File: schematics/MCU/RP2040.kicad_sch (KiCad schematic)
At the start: 37 parts, among them J2 Conn_ARM_SWD_TagConnect_TC203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, Q1 2N7002VC-7, SW1 SWITCH, U3 GD25LQ128DYIGR

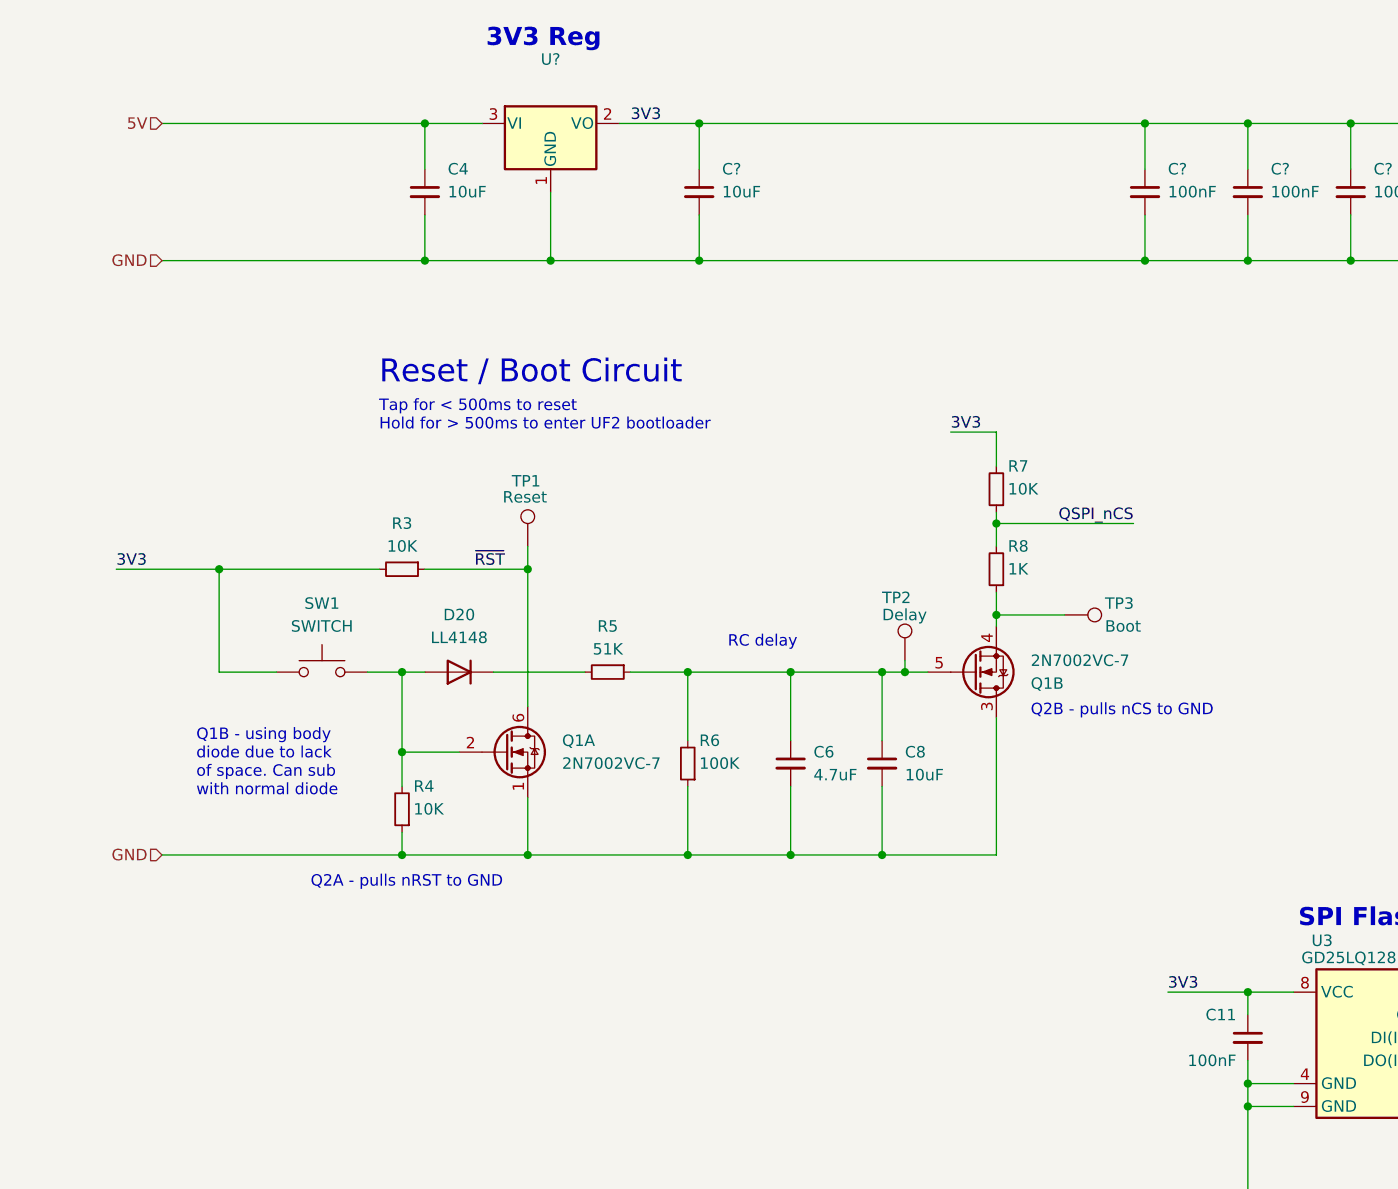
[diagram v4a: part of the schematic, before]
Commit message: copy used footprints into lib, link 3D models
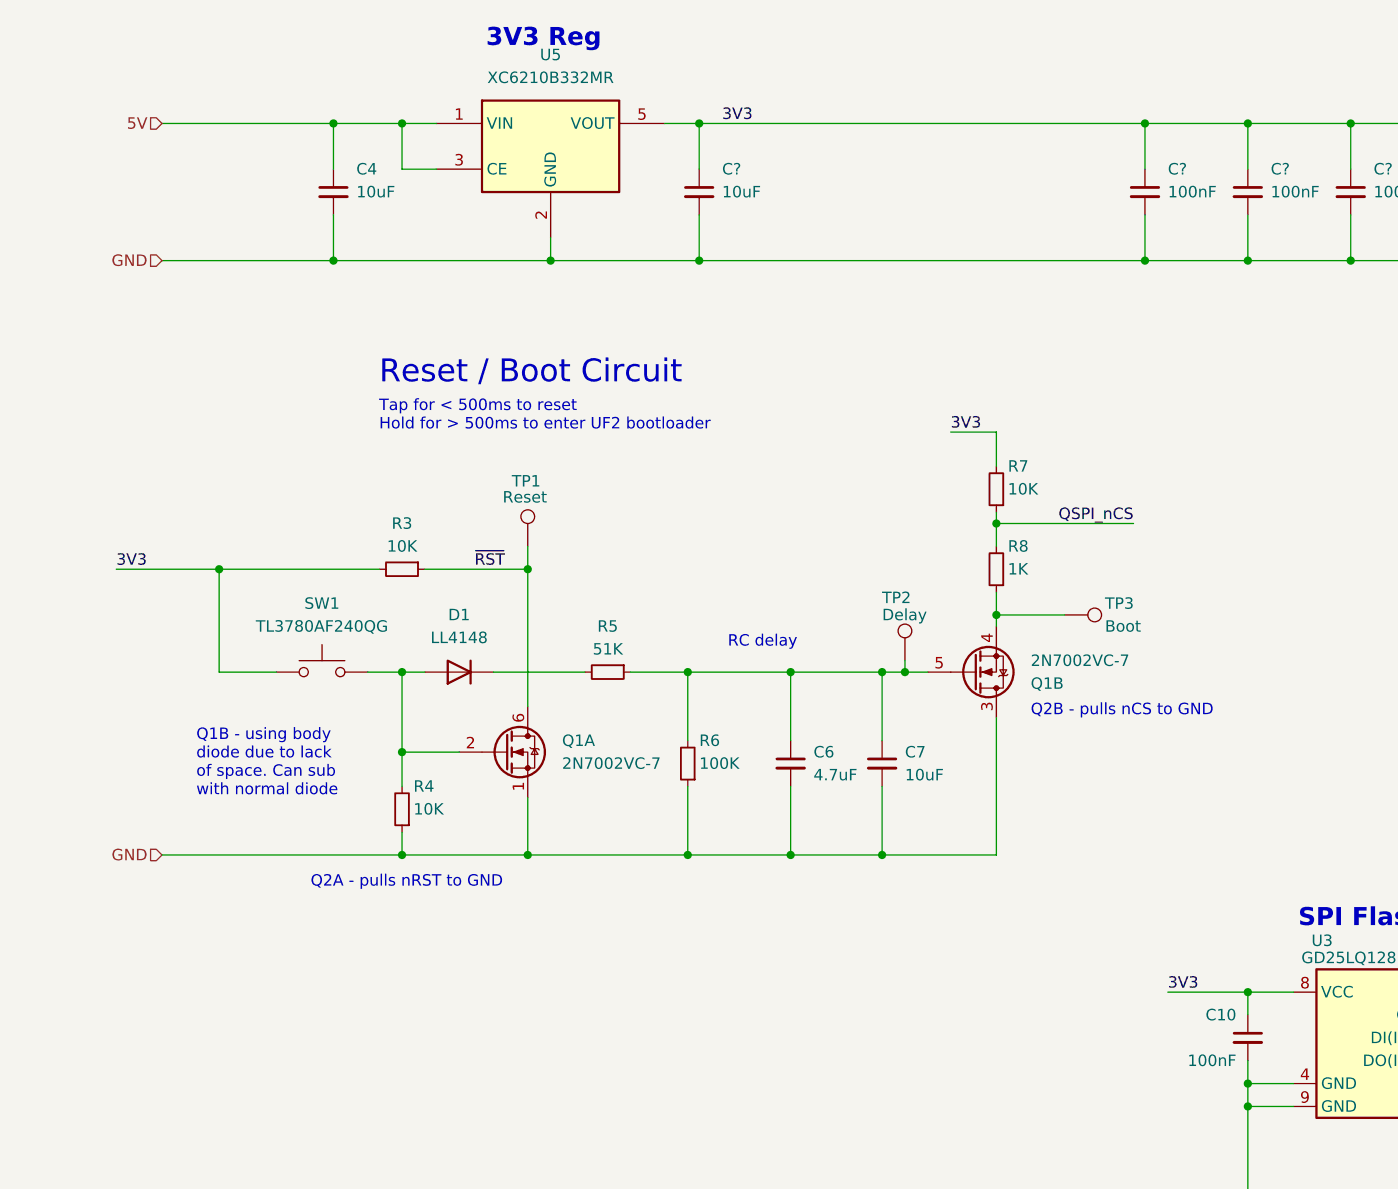
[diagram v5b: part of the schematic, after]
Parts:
- removed U?: XC6206PxxxMR-Regulator_Linear, Package_TO_SOT_SMD:SOT-23, symbol kicad-keyboard-parts:XC6206PxxxMR-Regulator_Linear
- added U5: XC6210B332MR, Package_TO_SOT_SMD:SOT-23-5, symbol Regulator_Linear:XC6210B332MR
- SW1: value SWITCH -> TL3780AF240QG; footprint (none) -> Mad_Footprints:SW_TL3780AF240QG; MPN (none) -> TL3780AF240QG; Manufacturer (none) -> E-Switch; Price (none) -> $0.41; Rating (none) -> SWITCH TACTILE SPST-NO 0.05A 12V; Supplier (none) -> Digikey; Supplier PN (none) -> EG5393CT-ND
- renumbered C11 to C10, C8 to C7, D20 to D1
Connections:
- net 5V: now also U5.1 (VIN), U5.3 (CE)
- net GND: now also U5.2 (GND)
- net IOVDD: now also U5.5 (VOUT)
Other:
- moved on the sheet: C4

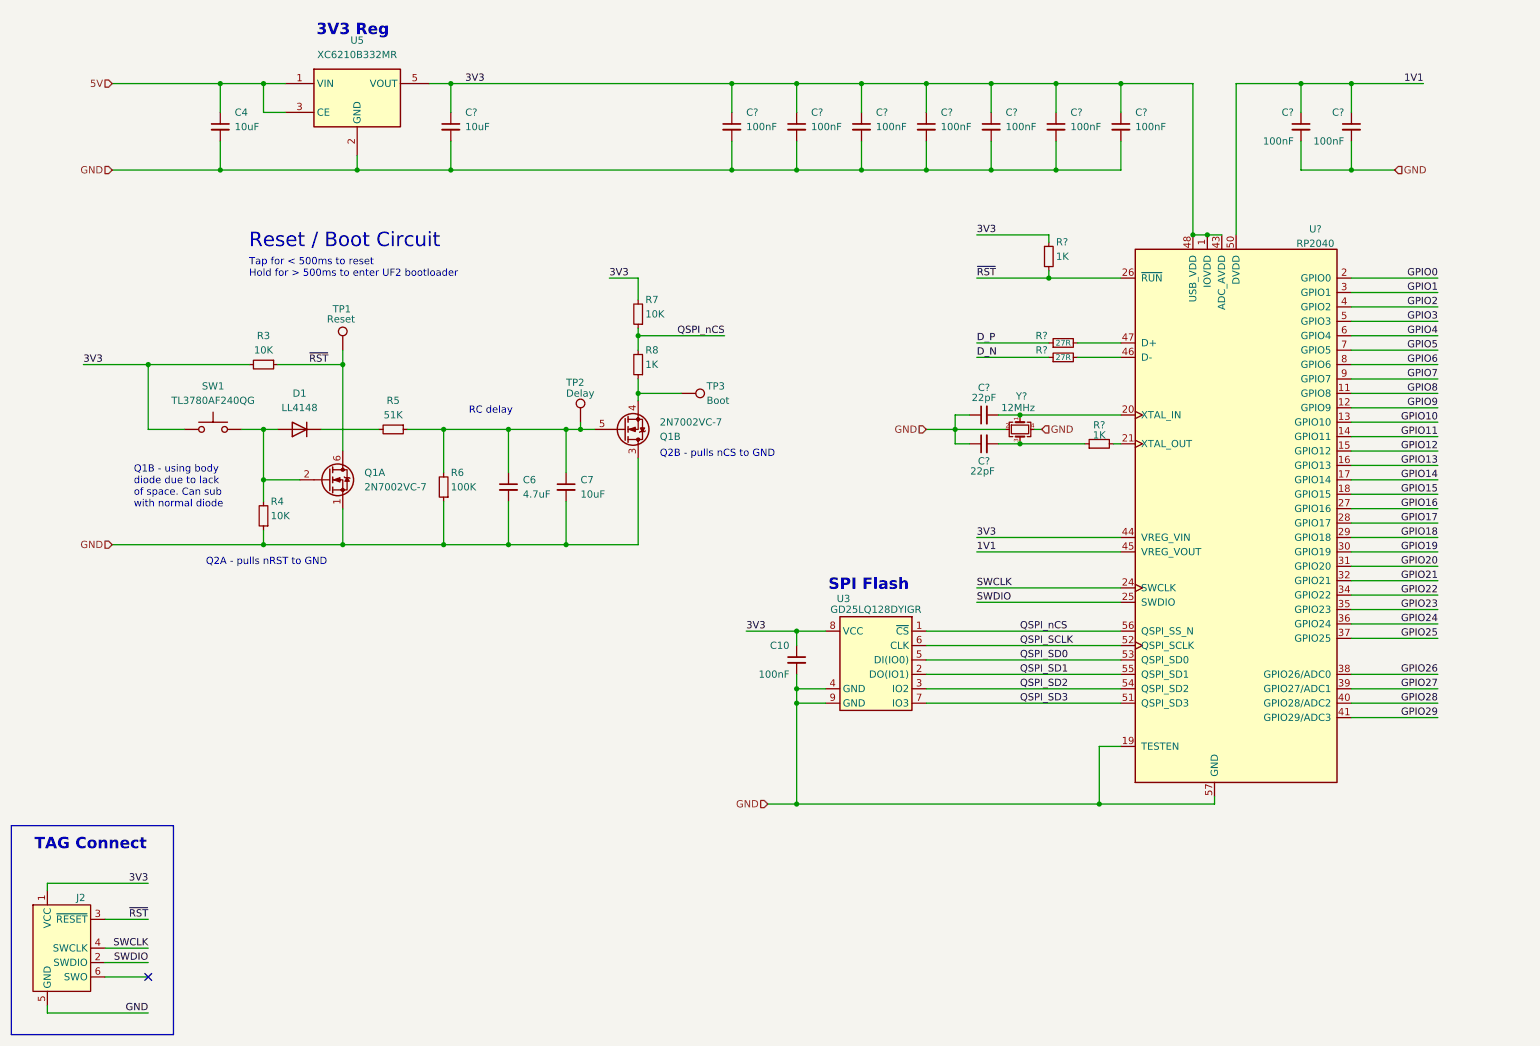
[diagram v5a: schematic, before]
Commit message: Update RP2040, rename bom only footprint, add mechanical footprint
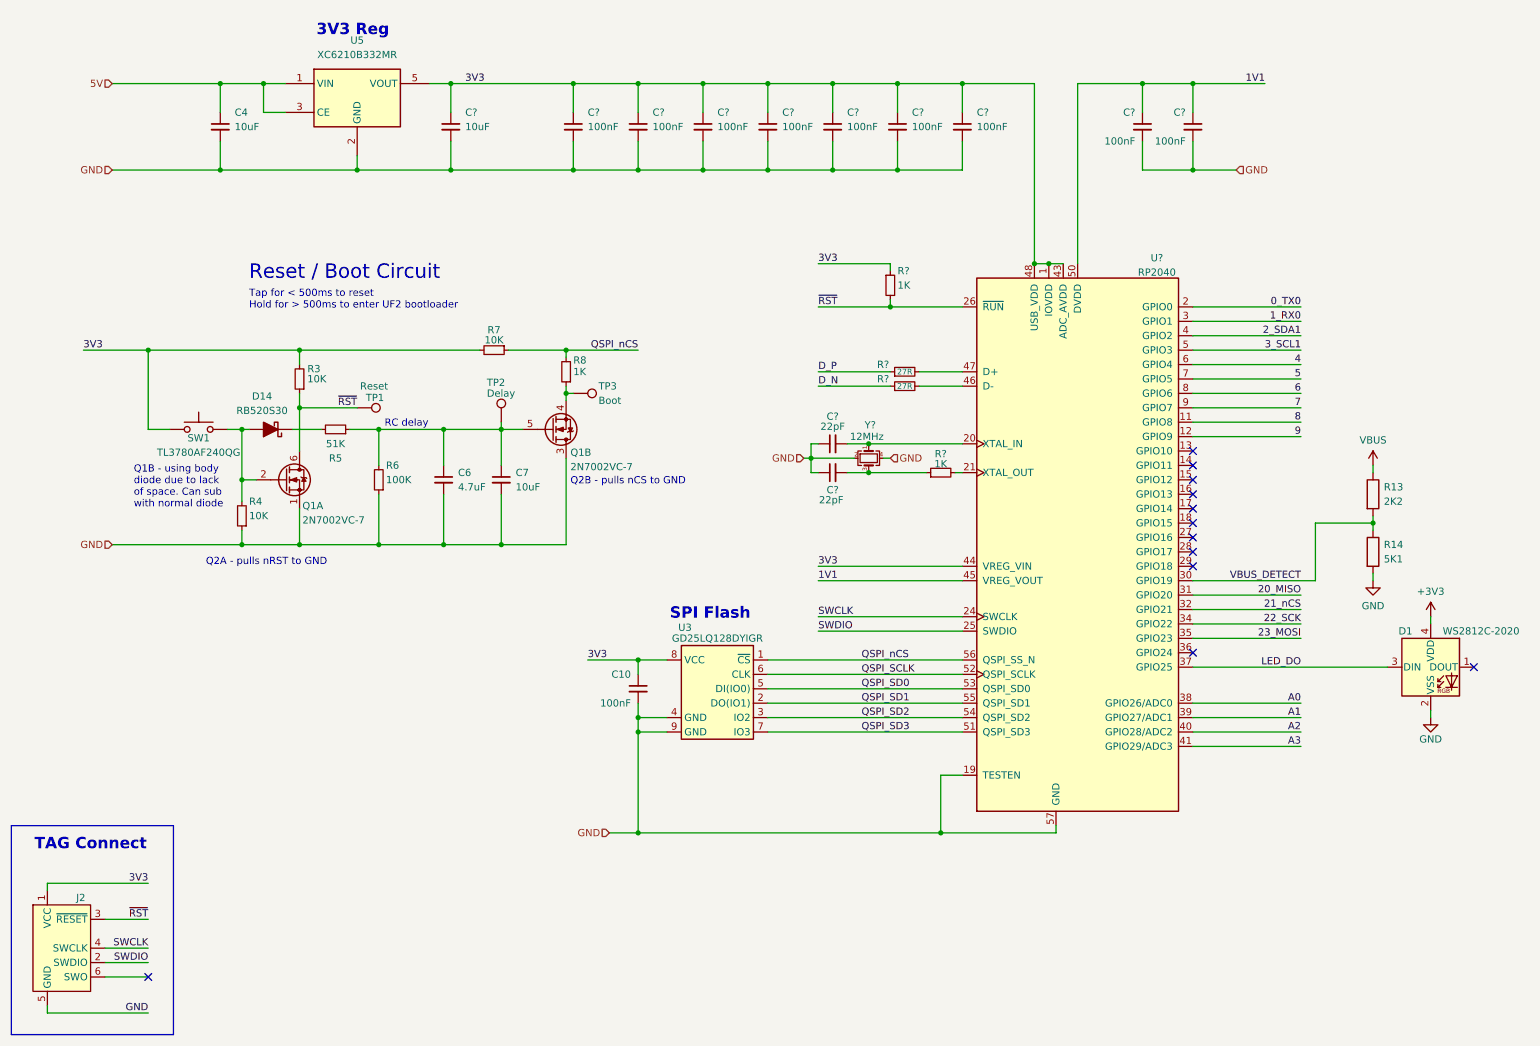
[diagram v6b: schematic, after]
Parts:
- removed D1: LL4148, Diode_SMD:D_MiniMELF, symbol Diode:LL4148
- added D1: WS2812C-2020, LED_SMD:LED_WS2812B-2020_PLCC4_2.0x2.0mm, symbol LED:WS2812B-2020
- added D14: RB520S30, Diode_SMD:D_SOD-523, symbol PCM_Diode_Schottky_AKL:RB520S30
- added R13: 2K2, Resistor_SMD:R_0402_1005Metric, symbol Device:R
- added R14: 5K1, Resistor_SMD:R_0402_1005Metric, symbol Device:R
- U3: symbol josh-memory:W25Q128JVSIQ -> Mad_Symbols:W25Q128JVSIQ
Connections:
- net GND: now also D1.2 (VSS), R14.2
- net at Q1.2 (G), R4.2, SW1.1: now also D14.2 (A)
- net at R5.2: now also D14.1 (K)
- net GPIO0 renamed 0_TX0
- net GPIO1 renamed 1_RX0
- net GPIO10: no longer names the net of U?.13 (GPIO10)
- net GPIO11: no longer names the net of U?.14 (GPIO11)
- net GPIO12: no longer names the net of U?.15 (GPIO12)
- net GPIO13: no longer names the net of U?.16 (GPIO13)
- net GPIO14: no longer names the net of U?.17 (GPIO14)
- net GPIO15: no longer names the net of U?.18 (GPIO15)
- net GPIO16: no longer names the net of U?.27 (GPIO16)
- net GPIO17: no longer names the net of U?.28 (GPIO17)
- net GPIO18: no longer names the net of U?.29 (GPIO18)
- net GPIO19 renamed VBUS_DETECT
- net VBUS_DETECT: now also R13.2, R14.1
- net GPIO2 renamed 2_SDA1
- net GPIO20 renamed 20_MISO
- net GPIO21 renamed 21_nCS
- net GPIO22 renamed 22_SCK
- net GPIO23 renamed 23_MOSI
- net GPIO24: no longer names the net of U?.36 (GPIO24)
- net GPIO25 renamed LED_DO
- net LED_DO: now also D1.3 (DIN)
- net GPIO26 renamed A0
- net GPIO27 renamed A1
- net GPIO28 renamed A2
- net GPIO29 renamed A3
- net GPIO3 renamed 3_SCL1
- net GPIO4 renamed 4
- net GPIO5 renamed 5
- net GPIO6 renamed 6
- net GPIO7 renamed 7
- net GPIO8 renamed 8
- net GPIO9 renamed 9
- new net +3V3: D1.4 (VDD)
- new net VBUS: R13.1
- no-connect marks 1 -> 12
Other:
- moved on the sheet: C10, C6, C7, C?, Q1A, Q1B, R3, R4, R5, R6, R7, R8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

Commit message: cleanup schematics and symbols
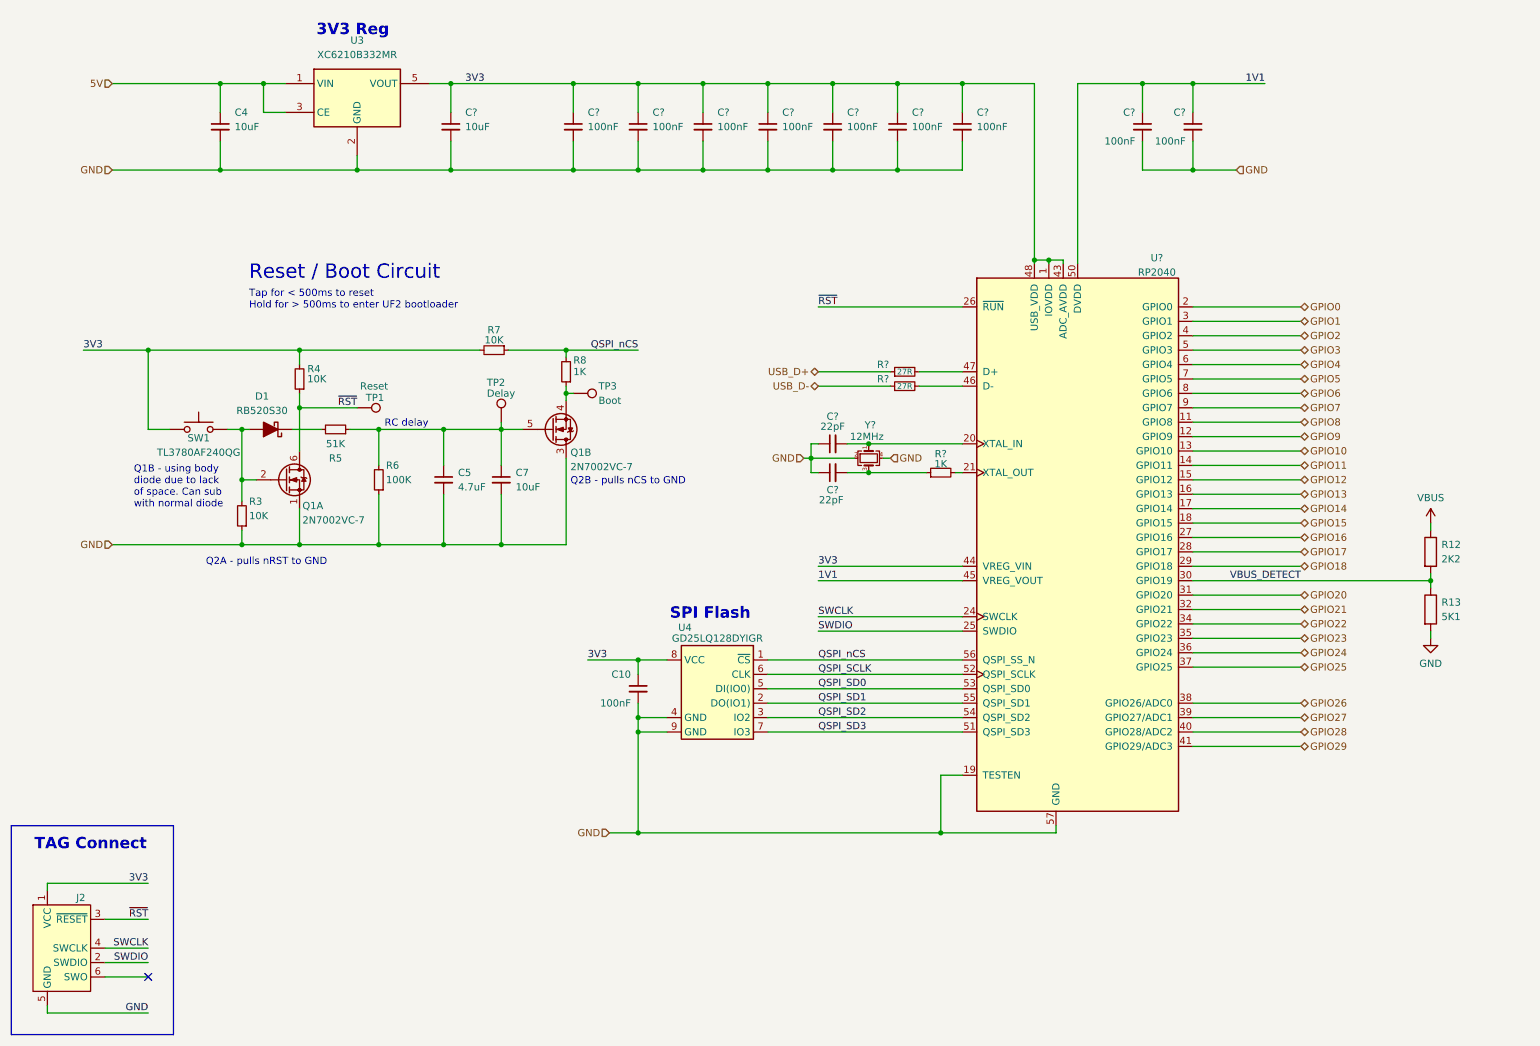
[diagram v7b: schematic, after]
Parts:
- removed D1: WS2812C-2020, LED_SMD:LED_WS2812B-2020_PLCC4_2.0x2.0mm, symbol LED:WS2812B-2020
- removed R?: 1K, Resistor_SMD:R_0402_1005Metric, symbol Device:R_Small
- U?: symbol Sleep-lib:RP2040 -> Mad_Symbols:RP2040
- renumbered C6 to C5, D14 to D1, R13 to R12, R14 to R13, R4 to R3, R3 to R4, U5 to U3, U3 to U4
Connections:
- net GPIO10: now reaches U?.13 (GPIO10)
- net GPIO11: now reaches U?.14 (GPIO11)
- net GPIO12: now reaches U?.15 (GPIO12)
- net GPIO13: now reaches U?.16 (GPIO13)
- net GPIO14: now reaches U?.17 (GPIO14)
- net GPIO15: now reaches U?.18 (GPIO15)
- net GPIO16: now reaches U?.27 (GPIO16)
- net GPIO17: now reaches U?.28 (GPIO17)
- net GPIO18: now reaches U?.29 (GPIO18)
- net GPIO24: now reaches U?.36 (GPIO24)
- net 0_TX0 renamed GPIO0
- net 1_RX0 renamed GPIO1
- net 20_MISO renamed GPIO20
- net 21_nCS renamed GPIO21
- net 22_SCK renamed GPIO22
- net 23_MOSI renamed GPIO23
- net 2_SDA1 renamed GPIO2
- net 3_SCL1 renamed GPIO3
- net 4 renamed GPIO4
- net 5 renamed GPIO5
- net 6 renamed GPIO6
- net 7 renamed GPIO7
- net 8 renamed GPIO8
- net 9 renamed GPIO9
- net A0 renamed GPIO26
- net A1 renamed GPIO27
- net A2 renamed GPIO28
- net A3 renamed GPIO29
- net DVDD renamed 1V1
- net D_N renamed USB_D-
- net D_P renamed USB_D+
- net IOVDD renamed 3V3
- net LED_DO renamed GPIO25
- no-connect marks 12 -> 1
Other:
- moved on the sheet: R12, R13

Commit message: add footprint for flash and 3d model
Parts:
- C7: footprint Capacitor_SMD:C_0402_1005Metric -> Capacitor_SMD:C_0805_2012Metric
- U4: value GD25LQ128DYIGR -> GD25Q127CWIGR; footprint Package_SON:WSON-8-1EP_6x5mm_P1.27mm_EP3.4x4mm -> Mad_Footprints:GD25LQ128DYIGR; MPN GD25LQ128DYIGR -> GD25Q127CWIGR; Supplier PN 1970-1088-1-ND -> 1970-1048-1-ND
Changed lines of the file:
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@@
 			)
 		)
-		(property "Value" "GD25LQ128DYIGR"
+		(property "Value" "GD25Q127CWIGR"
 			(at 140.97 125.73 0)
 			(effects
@@
 			)
 		)
-		(property "Footprint" "Package_SON:WSON-8-1EP_6x5mm_P1.27mm_EP3.4x4mm"
+		(property "Footprint" "Mad_Footprints:GD25LQ128DYIGR"
 			(at 137.16 134.62 0)
 			(effects
@@
 			)
 		)
-		(property "Description" "FLASH - NOR Memory IC 128Mbit SPI - Quad I/O 120 MHz 8-WSON (6x8)"
+		(property "Description" "FLASH - NOR Memory IC 128Mbit SPI - Quad I/O 104 MHz 8-WSON (5x6)"
 			(at 137.16 134.62 0)
 			(effects
@@
 			)
 		)
-		(property "Supplier PN" "1970-1088-1-ND"
+		(property "Supplier PN" "1970-1048-1-ND"
 			(at 137.16 134.62 0)
 			(effects
@@
 			)
 		)
-		(property "MPN" "GD25LQ128DYIGR"
+		(property "MPN" "GD25Q127CWIGR"
 			(at 137.16 134.62 0)
 			(effects
@@
 			)
 		)
-		(property "Footprint" "Capacitor_SMD:C_0402_1005Metric"
+		(property "Footprint" "Capacitor_SMD:C_0805_2012Metric"
 			(at 102.87 97.79 0)
 			(effects
